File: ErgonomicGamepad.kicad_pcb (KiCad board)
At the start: 2 copper layers, 86 parts, among them J1 USB_C_Receptacle_USB2.0_16P, J2 Conn_01x05, J3 Conn_01x05, J4 Conn_01x05, J5 AVR-ISP-6, J6 Conn_01x05, J7 1824417, SW01 SW_DIP_x01, SW02 SW_DIP_x01, SW03 SW_DIP_x01, SW04 SW_DIP_x01, SW05 SW_DIP_x01, SW06 SW_DIP_x01, SW07 SW_DIP_x01, SW08 SW_DIP_x01, SW09 SW_DIP_x01, SW10 SW_DIP_x01, SW11 SW_DIP_x01, SW12 SW_DIP_x01, SW13 SW_DIP_x01, SW14 SW_DIP_x01, SW15 SW_DIP_x01, SW16 SW_DIP_x01, SW17 SW_DIP_x01, SW18 SW_DIP_x01, SW19 SW_DIP_x01, SW20 SW_DIP_x01, SW21 SW_DIP_x01, SW22 SW_DIP_x01, SW23 SW_DIP_x01, SW24 SW_DIP_x01, U1 ATmega32U4-A, U2 USBLC6-2SC6, Y1 Crystal

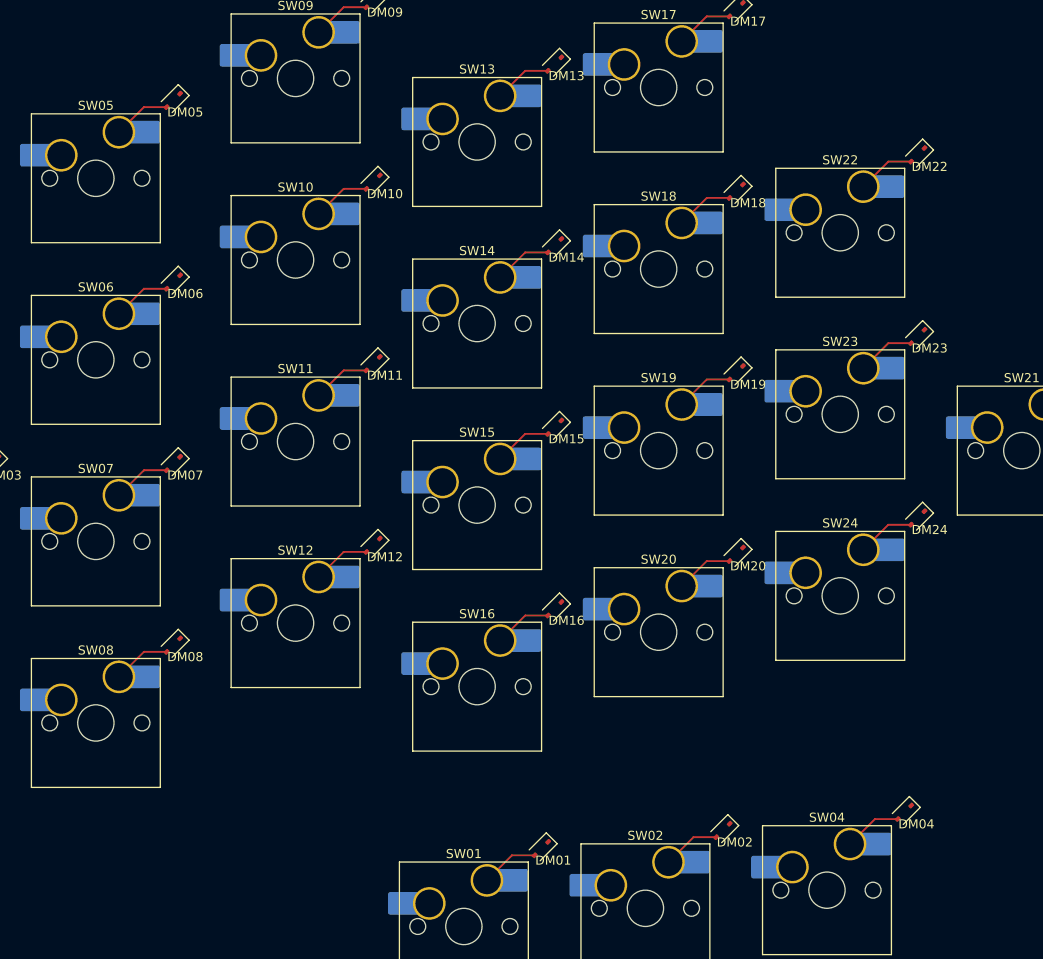
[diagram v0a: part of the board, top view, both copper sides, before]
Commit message: Split key matrix into Pinkie/Thumb satellite hierarchical sheets
Move satellite switches off the main schematic into their own sheets
and promote the crossing ROW/COL matrix nets to global labels so
connectivity survives the sheet boundary.
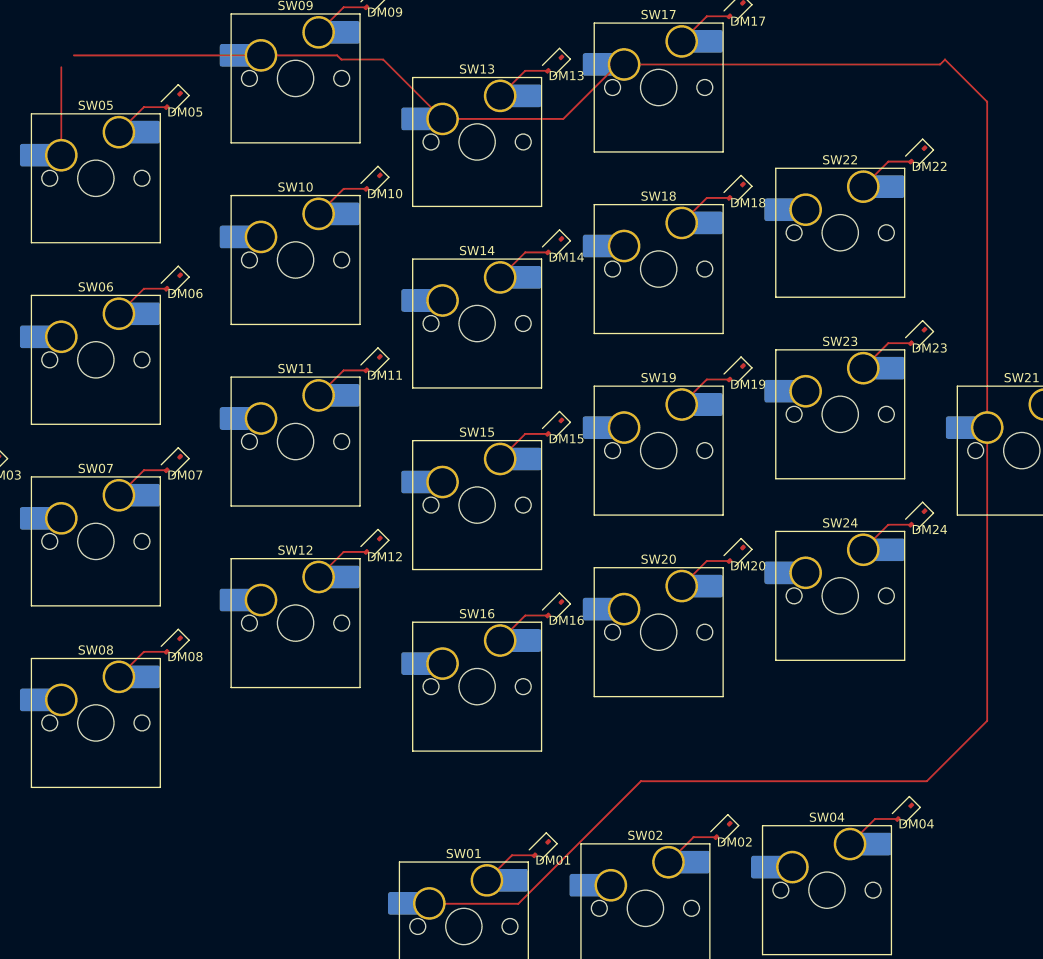
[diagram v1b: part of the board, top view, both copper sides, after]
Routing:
- net /ROW1: track 0.00 -> 257.6 mm
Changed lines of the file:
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@@
+	)
+	(segment
+		(start 199 138.5)
+		(end 209 138.5)
+		(width 0.2)
+		(layer "F.Cu")
+		(net "/ROW1")
+	)
+	(segment
+		(start 199.04 138.46)
+		(end 199 138.5)
+		(width 0.2)
+		(layer "F.Cu")
+		(net "/ROW1")
+	)
+	(segment
+		(start 213.96 52.04)
+		(end 200.65 52.04)
+		(width 0.2)
+		(layer "F.Cu")
+		(net "/ROW1")
+	)
+	(segment
+		(start 260.65 50.15)
+		(end 256 45.5)
+		(width 0.2)
+		(layer "F.Cu")
+		(net "/ROW1")
+	)
+	(segment
+		(start 199.19 138.46)
+		(end 199.04 138.46)
+		(width 0.2)
+		(layer "F.Cu")
+		(net "/ROW1")
+	)
+	(segment
+		(start 194.11 45.5)
+		(end 189.5 45.5)
+		(width 0.2)
+		(layer "F.Cu")
+		(net "/ROW1")
+	)
+	(segment
+		(start 260.65 86.04)
+		(end 260.65 50.15)
+		(width 0.2)
+		(layer "F.Cu")
+		(net "/ROW1")
+	)
+	(segment
+		(start 160.04 45.04)
+		(end 180.65 45.04)
+		(width 0.2)
+		(layer "F.Cu")
+		(net "/ROW1")
+	)
+	(segment
+		(start 189.04 45.04)
+		(end 180.65 45.04)
+		(width 0.2)
+		(layer "F.Cu")
+		(net "/ROW1")
+	)
+	(segment
+		(start 260.65 118.35)
+		(end 260.65 86.04)
+		(width 0.2)
+		(layer "F.Cu")
+		(net "/ROW1")
+	)
+	(segment
+		(start 220.65 46.04)
+		(end 219.96 46.04)
+		(width 0.2)
+		(layer "F.Cu")
+		(net "/ROW1")
+	)
+	(segment
+		(start 158.46 56.04)
+		(end 158 56.5)
+		(width 0.2)
+		(layer "F.Cu")
+		(net "/ROW1")
+	)
+	(segment
+		(start 209 138.5)
+		(end 222.5 125)
+		(width 0.2)
+		(layer "F.Cu")
+		(net "/ROW1")
+	)
+	(segment
+		(start 158.65 56.04)
+		(end 158.46 56.04)
+		(width 0.2)
+		(layer "F.Cu")
+		(net "/ROW1")
+	)
+	(segment
+		(start 256 45.5)
+		(end 255.46 46.04)
+		(width 0.2)
+		(layer "F.Cu")
+		(net "/ROW1")
+	)
+	(segment
+		(start 158 56.5)
+		(end 158.5 56.5)
+		(width 0.2)
+		(layer "F.Cu")
+		(net "/ROW1")
+	)
+	(segment
+		(start 255.46 46.04)
+		(end 220.65 46.04)
+		(width 0.2)
+		(layer "F.Cu")
+		(net "/ROW1")
+	)
+	(segment
+		(start 219.96 46.04)
+		(end 213.96 52.04)
+		(width 0.2)
+		(layer "F.Cu")
+		(net "/ROW1")
+	)
+	(segment
+		(start 254 125)
+		(end 260.65 118.35)
+		(width 0.2)
+		(layer "F.Cu")
+		(net "/ROW1")
+	)
+	(segment
+		(start 189.5 45.5)
+		(end 189.04 45.04)
+		(width 0.2)
+		(layer "F.Cu")
+		(net "/ROW1")
+	)
+	(segment
+		(start 158.65 56.04)
+		(end 158.65 46.35)
+		(width 0.2)
+		(layer "F.Cu")
+		(net "/ROW1")
+	)
+	(segment
+		(start 222.5 125)
+		(end 254 125)
+		(width 0.2)
+		(layer "F.Cu")
+		(net "/ROW1")
+	)
+	(segment
+		(start 200.65 52.04)
+		(end 194.11 45.5)
+		(width 0.2)
+		(layer "F.Cu")
+		(net "/ROW1")
 	)
 	(segment
